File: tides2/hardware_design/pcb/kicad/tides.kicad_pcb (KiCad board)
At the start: 2 copper layers, 69.2 x 107 mm, 181 parts, among them IC1 STM32F373CCT6, IC10 LM4040B10, IC2 4051PW, IC3 R-78E3.3-0.5, IC4 DAC8164ICPW, IC5 LD2981ABU33, IC6 MCP6004, IC7 MCP6004, IC8 TLV4172, IC9 TLV4172, J1 PJ301_THONKICONN6, J10 PJ301_THONKICONN6, J11 PJ301_THONKICONN6, J12 PJ301_THONKICONN6, J2 PJ301_THONKICONN6, J3 PJ301_THONKICONN6, J4 PJ301_THONKICONN6, J5 PJ301_THONKICONN6, J6 PJ301_THONKICONN6, J7 PJ301_THONKICONN6, J8 PJ301_THONKICONN6, J9 PJ301_THONKICONN6, Q1 8MHz

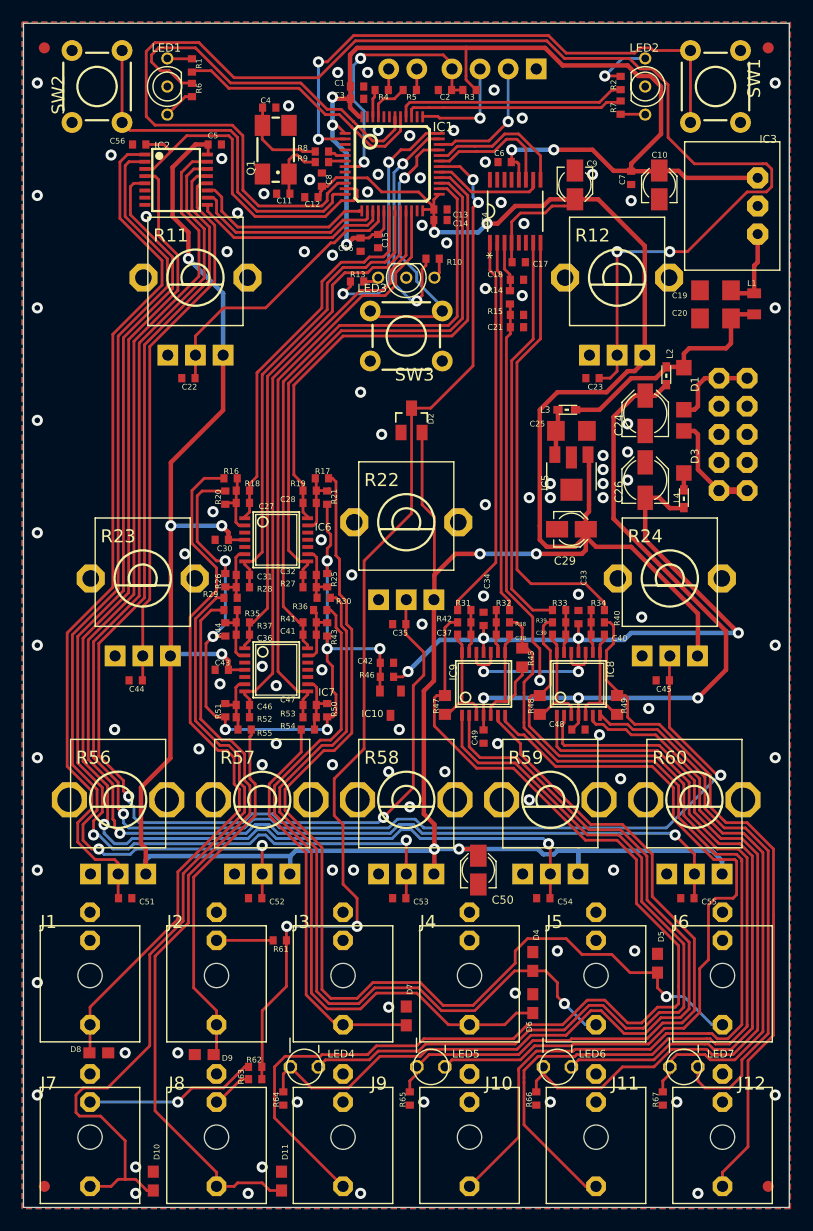
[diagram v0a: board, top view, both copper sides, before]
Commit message: replace tssop tlv op amp with soic
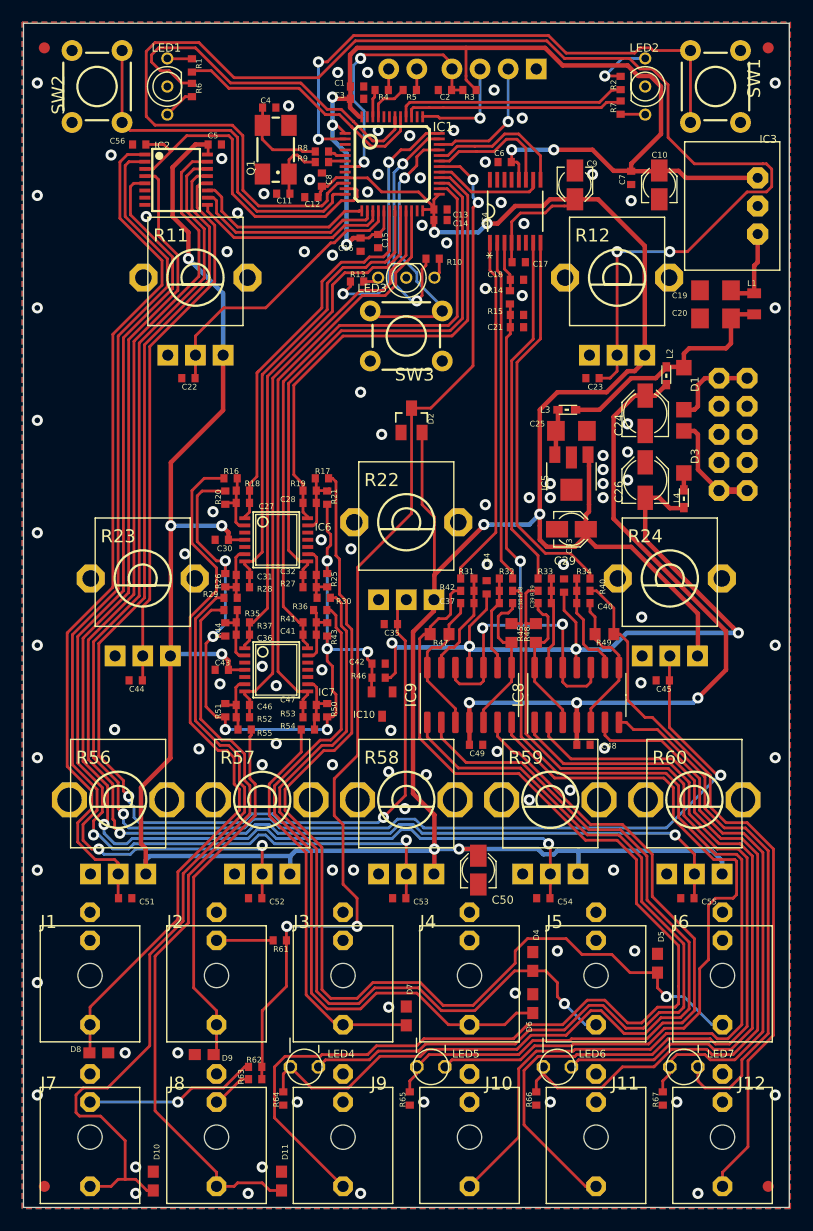
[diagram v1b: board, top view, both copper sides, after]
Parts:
- removed U$2: , tides:ROHS_BIG
- removed U$4: , tides:CE_MEDIUM
- removed U$5: , tides:FCC_MEDIUM
- IC8, IC9: footprint tides:TSSOP14_065 -> Package_SO:SOIC-14_3.9x8.7mm_P1.27mm
- JP6: value (none) -> M04PTH
- JP7: value (none) -> M02PTH
- L2, L3, L4: value (none) -> WE-CBF_0603
- SW1, SW2, SW3: value (none) -> TAC_SWITCHPTH
- moved R48 6.51 mm to (160.2, 106.6)
- moved R49 6.50 mm to (166.4, 106.7), turned to 180 degrees
- moved R47 6.42 mm to (151.5, 106.7), turned to 0 degrees
- moved C33 3.13 mm to (162.7, 102.3)
- moved R33 3.13 mm to (161.0, 101.7)
- moved C39 3.13 mm to (161.0, 103.9)
- moved C40 3.13 mm to (164.5, 103.9)
- moved R39 3.13 mm to (161.0, 102.8)
- moved R40 3.13 mm to (164.5, 102.8)
- moved R34 3.13 mm to (164.5, 101.7)
- moved C38 2.86 mm to (157.5, 103.9)
- moved C34 2.86 mm to (155.8, 102.5)
- moved R31 2.86 mm to (154.0, 101.7)
- moved R42 2.86 mm to (154.0, 102.8)
- moved C37 2.86 mm to (154.0, 103.9)
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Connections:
- net CLOCK_IN renamed Net-(D11-Pad2)
- net DAC_1 renamed /tides_5/DAC_1
- net DAC_2 renamed /tides_5/DAC_2
- net DAC_3 renamed /tides_5/DAC_3
- net DAC_4 renamed /tides_5/DAC_4
- net FM_IN renamed Net-(D9-Pad2)
- net FREQUENCY_ATT renamed /tides_3/FREQUENCY_ATT
- net RESET renamed /tides_2/RESET
- net RX renamed /tides_2/RX
- net SHAPE_ATT renamed /tides_3/SHAPE_ATT
- net SHAPE_IN renamed Net-(D4-Pad2)
- net SHIFT_ATT renamed /tides_3/SHIFT_ATT
- net SHIFT_IN renamed Net-(D5-Pad2)
- net SHIFT_POT renamed /tides_3/SHIFT_POT
- net SLOPE_ATT renamed /tides_3/SLOPE_ATT
- net SLOPE_IN renamed Net-(D8-Pad2)
- net SLOPE_POT renamed /tides_3/SLOPE_POT
- net SMOOTHNESS_ATT renamed /tides_3/SMOOTHNESS_ATT
- net SMOOTHNESS_IN renamed Net-(D6-Pad2)
- net SMOOTHNESS_POT renamed /tides_3/SMOOTHNESS_POT
- net SWCLK renamed /tides_2/SWCLK
- net SWDIO renamed /tides_2/SWDIO
- net TRIG_IN renamed Net-(D10-Pad2)
- net TX renamed /tides_2/TX
- net VREF renamed /tides_5/VREF
- net VREF_BIAS renamed /tides_5/VREF_BIAS
- net V_OCT_IN renamed Net-(D7-Pad2)
- IC1 pad 3: (no net) -> unconnected-(IC1-Pad3)
- IC1 pad 38: (no net) -> unconnected-(IC1-Pad38)
- IC1 pad 4: (no net) -> unconnected-(IC1-Pad4)
- IC1 pad 43: (no net) -> unconnected-(IC1-Pad43)
- J10 pad P2: (no net) -> unconnected-(J10-PadP2)
- J11 pad P2: (no net) -> unconnected-(J11-PadP2)
- J12 pad P2: (no net) -> unconnected-(J12-PadP2)
- J9 pad P2: (no net) -> unconnected-(J9-PadP2)
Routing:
- net VEE: track 57.8 -> 70.5 mm
- net Net-(J9-PadP3): track 102.9 -> 108.6 mm
- net Net-(C40-Pad1): track 3.92 -> 9.62 mm
- net Net-(C37-Pad1): track 3.92 -> 9.51 mm
- net /tides_5/DAC_4: track 40.2 -> 35.3 mm
- net Net-(C38-Pad1): track 3.92 -> 8.66 mm
- net /tides_5/DAC_3: track 36.6 -> 32.1 mm
- net Net-(C39-Pad1): track 3.92 -> 8.31 mm
- net Net-(J10-PadP3): track 87.3 -> 91.1 mm
- net Net-(J11-PadP3): track 89.0 -> 92.3 mm
- net +3V3_A: track 323.3 -> 320.2 mm
- net VCC: track 62.0 -> 65.1 mm
- net /tides_5/DAC_1: track 34.8 -> 31.9 mm
- net Net-(C37-Pad2): track 10.6 -> 13.5 mm
- net Net-(C40-Pad2): track 10.6 -> 13.3 mm
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
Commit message: tides2 cleanup
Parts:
- moved C42 1.20 mm to (145.7, 108.2)
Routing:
- net VCC: track 65.1 -> 52.3 mm
- net VEE: track 70.5 -> 57.9 mm
- net +3V3_A: track 320.2 -> 318.3 mm, vias 10 -> 12
- net SW_MODE: track 25.5 -> 23.7 mm
- net AREF_-10: track 70.3 -> 71.6 mm
- net /tides_3/SMOOTHNESS_POT: track 109.9 -> 108.8 mm
- net Net-(C20-Pad1): track 22.0 -> 21.2 mm
- net Net-(D7-Pad2): track 36.8 -> 36.0 mm
- net LED_RANGE_G: track 33.1 -> 32.4 mm
- net Net-(C28-Pad1): track 6.42 -> 5.76 mm
- net Net-(J10-PadP3): track 91.1 -> 90.5 mm
- net SW_SHIFT: track 52.1 -> 51.5 mm
- net Net-(D10-Pad2): track 73.8 -> 73.3 mm
- net /tides_2/RESET: track 24.0 -> 23.5 mm
- net GND: vias 101 -> 103

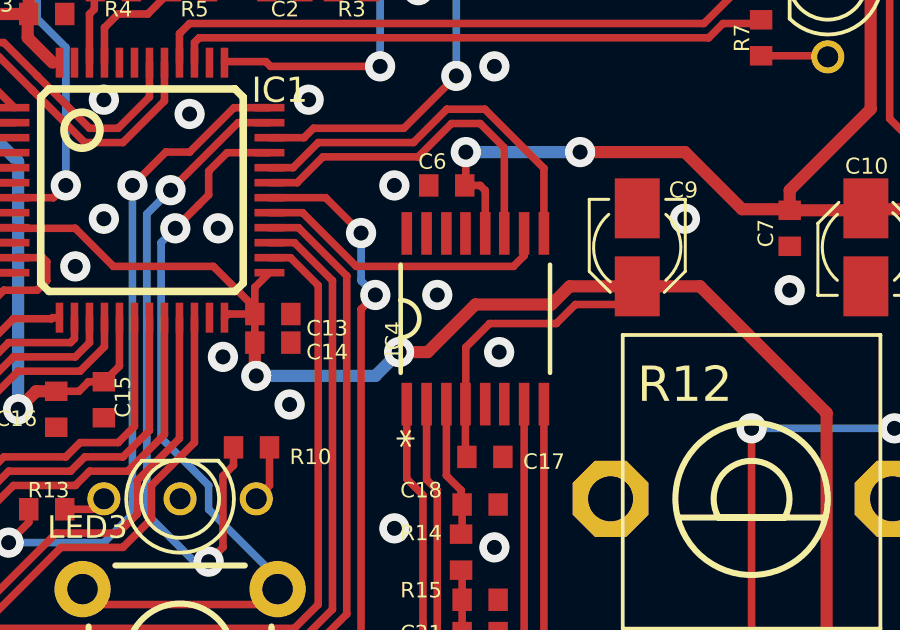
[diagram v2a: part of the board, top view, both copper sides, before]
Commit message: tides2 dac8164 -> dac8565
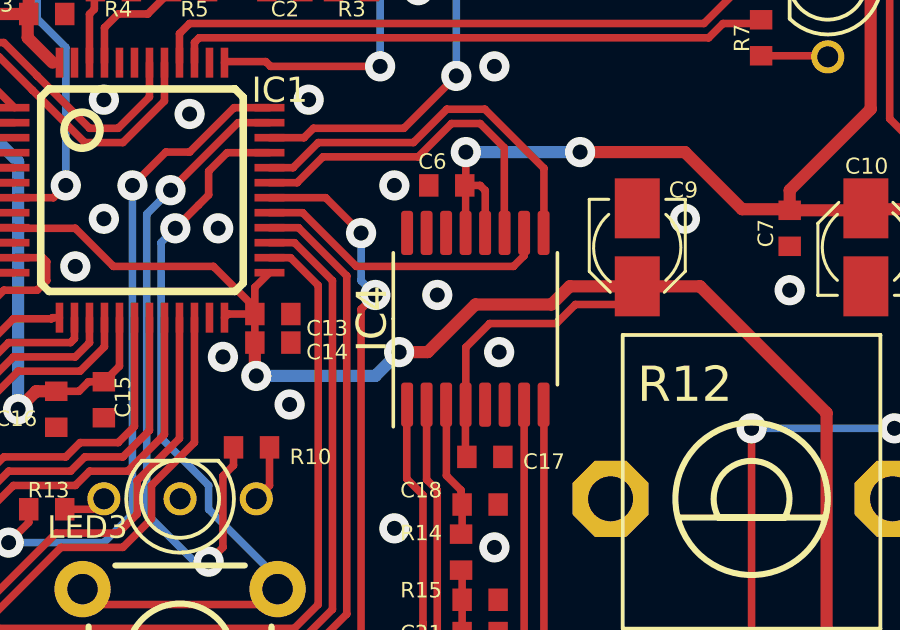
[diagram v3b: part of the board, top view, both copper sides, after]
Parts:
- IC4: value DAC8164ICPW -> DAC8565; footprint tides:SOP65P640X110-16N -> Package_SO:TSSOP-16_4.4x5mm_P0.65mm
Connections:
- IC4 pad 13: GND -> +3V3
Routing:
- net +3V3: track 97.9 -> 99.5 mm

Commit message: tides final tweaks
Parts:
- C10, C29, C50, C9: footprint tides:PANASONIC_A -> tides:PANASONIC_B
- moved C7 0.66 mm to (168.2, 65.4)
- moved C10 0.42 mm to (170.9, 66.1)
- moved C24 0.27 mm to (169.8, 86.8)
- moved C29 0.26 mm to (163.7, 97.2)
- moved C26 0.25 mm to (169.8, 92.8)
- moved C50 0.13 mm to (155.0, 127.9)
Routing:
- net +3V3_A: track 318.3 -> 319.0 mm
- net /tides_5/DAC_4: track 35.3 -> 35.9 mm
